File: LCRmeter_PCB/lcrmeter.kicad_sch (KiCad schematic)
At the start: 60 parts, among them J1 LCR_input, J2 LCR_input, J3 Prog_interface, J4 USB_B_Micro, J5 OSCILLOSCOPE, J6 misc, J7 misc, SW1 power, SW2 +, SW3 -, SW4 ok, SW5 back, U3 OLED, U4 74HC14, U5 MCP6001-OT, U6 STM32G473C_B-C-E_Tx, Y1 8Mhz

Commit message: some random schematic update
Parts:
- removed D1: 2V, Diode_SMD:D_MiniMELF, symbol Device:D_Zener
- removed J5: OSCILLOSCOPE, footprints:BNC TE CONNECTIVITY 5-1634503, symbol Connector:Conn_Coaxial
- removed R3: 10k, Resistor_SMD:R_0603_1608Metric_Pad1.05x0.95mm_HandSolder, symbol Device:R_Small
- removed R7: R, symbol Device:R
- added C16: 10u, Capacitor_SMD:C_0603_1608Metric_Pad1.05x0.95mm_HandSolder, symbol Device:C
- added C17: C_Polarized_Small, symbol Device:C_Polarized_Small
- added Q1: NX7002BKR, Package_TO_SOT_SMD:SOT-23, symbol Transistor_FET:2N7002
- added R20, R21, R8: 0, symbol Device:R
- added TP1, TP2, TP3: TestPoint, symbol Connector:TestPoint
- added U1, U2, U7: 74LVC1G66, symbol 74xGxx:74LVC1G66
- added U8: MCP6001-OT, Package_TO_SOT_SMD:SOT-23-5, symbol Amplifier_Operational:MCP6001-OT
- R17: value 10k -> 0; footprint Resistor_SMD:R_0603_1608Metric_Pad1.05x0.95mm_HandSolder -> (none)
- R18: value 10k -> 2k; footprint Resistor_SMD:R_0603_1608Metric_Pad1.05x0.95mm_HandSolder -> (none)
- R19: value 20k -> 500; footprint Resistor_SMD:R_0805_2012Metric_Pad1.15x1.40mm_HandSolder -> (none)
- R22, R23: footprint Resistor_SMD:R_0603_1608Metric_Pad1.05x0.95mm_HandSolder -> (none)
- SW2: value + -> up
- SW3: value - -> down
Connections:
- net +1V5: now also R21.2, R8.2, U8.1, U8.4 (-); no longer J1.3 (Pin_3), J1.4 (Pin_4), J2.3 (Pin_3), J2.4 (Pin_4), J6.4 (Pin_4), J7.4 (Pin_4), U5.1, U5.4 (-)
- net ADC_1: now also R18.1, R19.1, U5.1, U5.4 (-), R20.2, TP1.1, U7.1
- net ADC_2: now also Q1.3 (D), TP2.1, U1.2, U2.2, U7.2
- net GND: now also R17.2, R23.1, U6.19 (VSSA), U6.23 (VSS), U6.35 (VSS), U6.47 (VSS), Q1.2 (S), U1.3 (GND), U2.3 (GND), U8.2 (V-); no longer R18.2, R2.1, R23.2
- net OSCILLOSCOPE: no longer R17.2, R18.1
- net OSCILLOSCOPE_IN: now also J6.5 (Pin_5), J7.5 (Pin_5); no longer J6.3 (Pin_3), J7.3 (Pin_3), R17.1
- net PWM_OUT: now also J6.3 (Pin_3), J7.3 (Pin_3); no longer J6.1 (Pin_1), J7.1 (Pin_1)
- net RST: now also U6.7 (PG10)
- net USB_+: now also U6.34 (PA12)
- net USB_-: now also U6.33 (PA11)
- net VCC: now also J6.1 (Pin_1), J7.1 (Pin_1), R22.2, U6.1 (VBAT), U6.24 (VDD), U6.36 (VDD), U6.48 (VDD), U1.5 (VCC), U2.5 (VCC), U8.5 (V+); no longer J6.5 (Pin_5), J7.5 (Pin_5), R19.1, R22.1
- net VDDA: now also U6.21 (VDDA)
- net at C2.1, Y1.1: now also U6.5 (PF0)
- net at C1.1, Y1.2: now also U6.6 (PF1)
- net at R19.2: now also U1.1
- net at R2.2: now also U6.45 (PB8)
- net DAC_UNBUFFERED: now reaches U6.12 (PA4)
- net DAC_UNBUFFERED: now also U5.3 (+), R20.1
- net WAVE_OUT: now reaches U6.14 (PA6)
- net WAVE_OUT: now also J6.4 (Pin_4), J7.4 (Pin_4)
- net EVENTOUT: now reaches U6.2 (PC13)
- net EVENTOUT: now also TP3.1
- new net: J1.3 (Pin_3), J1.4 (Pin_4), J2.3 (Pin_3), J2.4 (Pin_4), R17.1, R8.1
- new net: R21.1, R22.1, R23.2, U8.3 (+)
- new net: R18.2, U2.1
- new net EN_PATH_1: U1.4
- new net EN_PATH_2: U2.4, U7.4
- new net RES_CALIBRATION: Q1.1 (G)
- no-connect marks 13 -> 12
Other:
- note added: "Use dac buffered, if uc's internal is not enough Use other paths for measurments if needed use Vdd/2 voltage reference if needed?"
- note removed: "Optional"
- moved on the sheet: C1, C10, C12, C13, C14, C15, C2, J1, J2, J7, R1, R10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

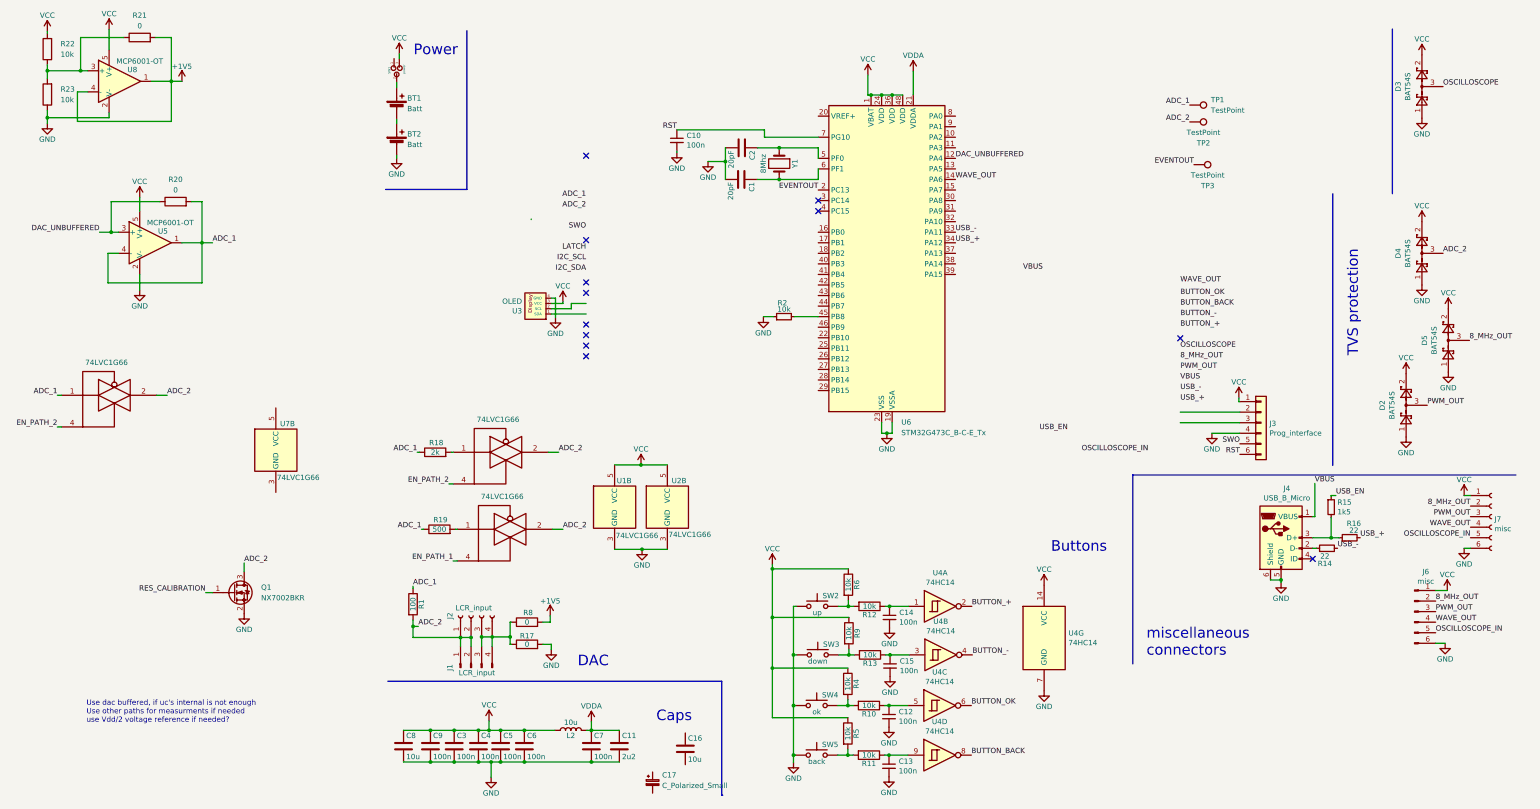
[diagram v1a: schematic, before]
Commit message: schematic done added generator for g4
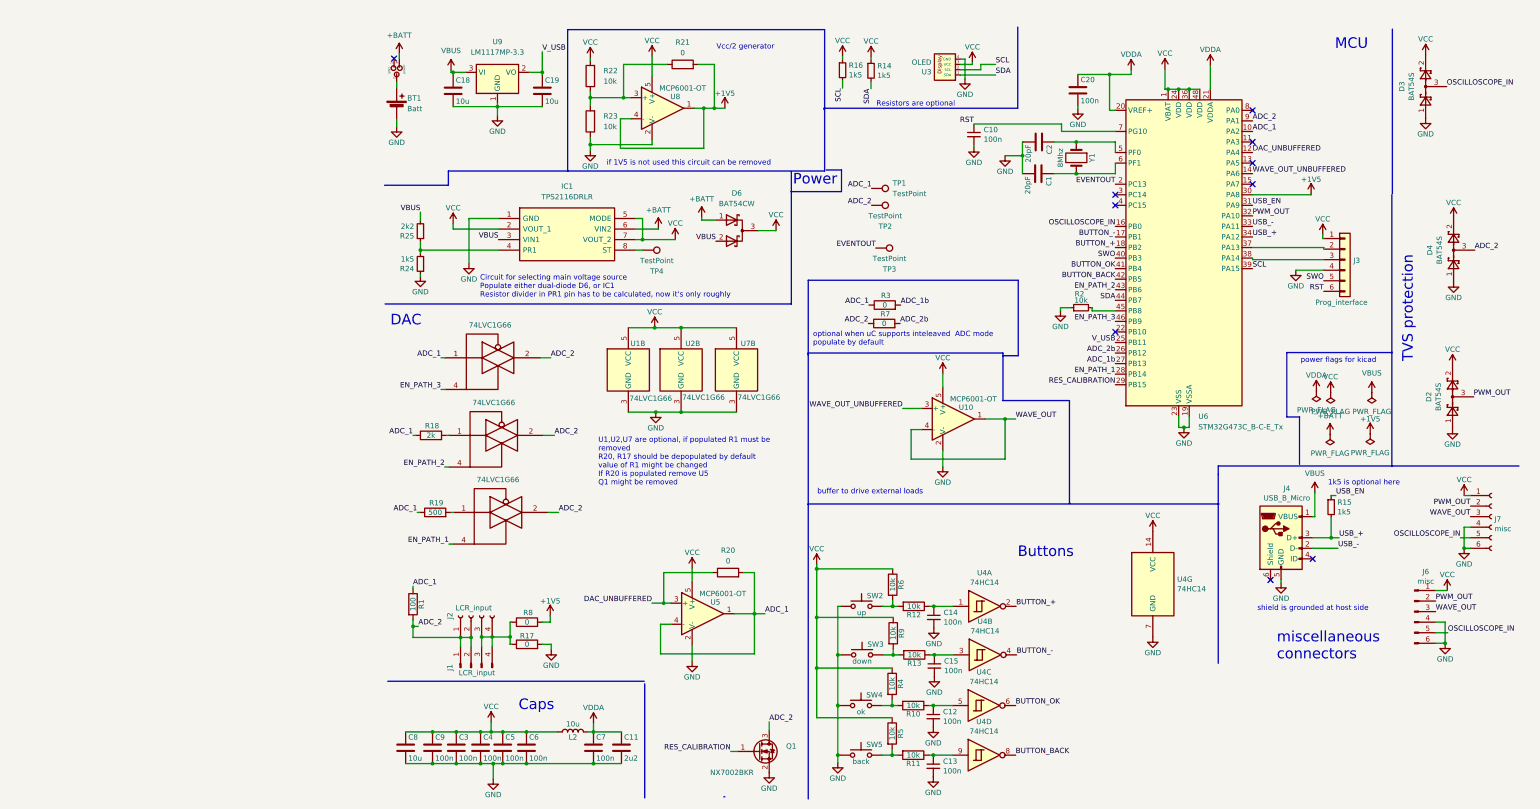
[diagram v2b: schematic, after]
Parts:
- removed BT2: Batt, Battery:BatteryHolder_Keystone_2466_1xAAA, symbol Device:Battery_Cell
- removed C16: 10u, Capacitor_SMD:C_0603_1608Metric_Pad1.05x0.95mm_HandSolder, symbol Device:C
- removed C17: C_Polarized_Small, symbol Device:C_Polarized_Small
- removed D5: BAT54S, Package_TO_SOT_SMD:SOT-23, symbol lcrmeter-rescue:BAT54S-Diode
- added C18, C19: 10u, Capacitor_SMD:C_0603_1608Metric_Pad1.05x0.95mm_HandSolder, symbol Device:C
- added C20: 100n, Capacitor_SMD:C_0603_1608Metric_Pad1.05x0.95mm_HandSolder, symbol Device:C
- added D6: BAT54CW, symbol Device:D_Schottky_Dual_CommonCathode_AAK_Parallel
- added IC1: TPS2116DRLR, SOTFL50P160X60-8N, symbol library_loader:TPS2116DRLR
- added R24: 1k5, Resistor_SMD:R_0805_2012Metric_Pad1.15x1.40mm_HandSolder, symbol Device:R_Small
- added R25: 2k2, Resistor_SMD:R_0805_2012Metric_Pad1.15x1.40mm_HandSolder, symbol Device:R_Small
- added R3, R7: 0, symbol Device:R
- added TP4: TestPoint, symbol Connector:TestPoint
- added U10: MCP6001-OT, Package_TO_SOT_SMD:SOT-23-5, symbol Amplifier_Operational:MCP6001-OT
- added U9: LM1117MP-3.3, Package_TO_SOT_SMD:SOT-223-3_TabPin2, symbol Regulator_Linear:LM1117MP-3.3
- R14, R16: value 22 -> 1k5
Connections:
- net 8_MHz_OUT is gone; now on net PWM_OUT: J6.2 (Pin_2), J7.2 (Pin_2)
- net OSCILLOSCOPE is gone; now on net OSCILLOSCOPE_IN: D3.3
- net +1V5: now also U6.30 (PA8)
- net ADC_1: now also U6.10 (PA2), R3.1
- net ADC_2: now also U6.9 (PA1), R7.1
- net BUTTON_+: now also U6.18 (PB2)
- net BUTTON_-: now also U6.17 (PB1)
- net BUTTON_BACK: now also U6.42 (PB5)
- net BUTTON_OK: now also U6.41 (PB4)
- net EN_PATH_1: now also U6.28 (PB14)
- net EN_PATH_2: now also U6.43 (PB6); no longer U7.4
- net GND: now also BT1.2 (-), J6.4 (Pin_4), J7.4 (Pin_4), R2.1, U7.3 (GND), C18.2, C19.2, C20.2, IC1.1 (GND), R24.1, U10.2 (V-), U9.1 (GND); no longer J4.6 (Shield)
- net OSCILLOSCOPE_IN: now also U6.16 (PB0)
- net PWM_OUT: now also U6.32 (PA10); no longer J6.3 (Pin_3), J7.3 (Pin_3)
- net RES_CALIBRATION: now also U6.29 (PB15)
- net SWO: now also U6.40 (PB3)
- net USB_+: now also J4.3 (D+), R15.2; no longer R16.2
- net USB_-: now also J4.2 (D-); no longer R14.2
- net USB_EN: now also U6.31 (PA9)
- net VBUS: now also C18.1, D6.2 (K), IC1.3 (VIN1), R25.2, U9.3 (VI)
- net VCC: now also R14.1, R16.1, U7.5 (VCC), D6.3 (A), IC1.2 (VOUT_1), IC1.5 (MODE), IC1.7 (VOUT_2), U10.5 (V+); no longer SW1.3
- net VDDA: now also U6.20 (VREF+), C20.1
- net WAVE_OUT: now also J6.3 (Pin_3), J7.3 (Pin_3), U10.1, U10.4 (-); no longer J6.4 (Pin_4), J7.4 (Pin_4), U6.14 (PA6)
- net at J3.2 (Pin_2): now also U6.37 (PA13)
- net at J3.3 (Pin_3): now also U6.38 (PA14)
- net SDA: now reaches U3.1 (SDA)
- net SDA: now also R14.2, U6.44 (PB7)
- net SCL: now reaches U3.2 (SCL)
- net SCL: now also R16.2, U6.39 (PA15)
- net V_USB: now reaches U6.25 (PB11)
- net V_USB: now also C19.1, U9.2 (VO)
- net ADC_2b: now reaches U6.26 (PB12)
- net ADC_2b: now also R7.2
- net ADC_1b: now reaches U6.27 (PB13)
- net ADC_1b: now also R3.2
- net EN_PATH_3: now reaches U6.46 (PB9)
- net EN_PATH_3: now also U7.4
- new net: IC1.4 (PR1), R24.2, R25.1
- new net: IC1.8 (ST), TP4.1
- new net +BATT: D6.1 (K), IC1.6 (VIN2), SW1.3
- new net WAVE_OUT_UNBUFFERED: U10.3 (+), U6.14 (PA6)
- no-connect marks 12 -> 10
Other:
- note added: "1k5 is optional here"
- note added: "Circuit for selecting main voltage source Populate either dual-diode D6, or IC1 Resistor divider in PR1 pin has to be calculated, now it's only roughly"
- note added: "MCU"
- note added: "Resistors are optional"
- note added: "U1,U2,U7 are optional, if populated R1 must be removed R20, R17 should be depopulated by default value of R1 might be changed If R20 is populated remove U5 Q1 might be removed"
- note added: "Vcc/2 generator"
- note added: "buffer to drive external loads"
- note added: "if 1V5 is not used this circuit can be removed"
- note added: "optional when uC supports inteleaved ADC mode populate by default"
- note added: "power flags for kicad"
- note added: "shield is grounded at host side"
- note removed: "Use dac buffered, if uc's internal is not enough Use other paths for measurments if needed use Vdd/2 voltage reference if needed?"
- moved on the sheet: C1, C10, C11, C12, C13, C14, C15, C2, C3, C4, C5, C6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

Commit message: placed components on PCB
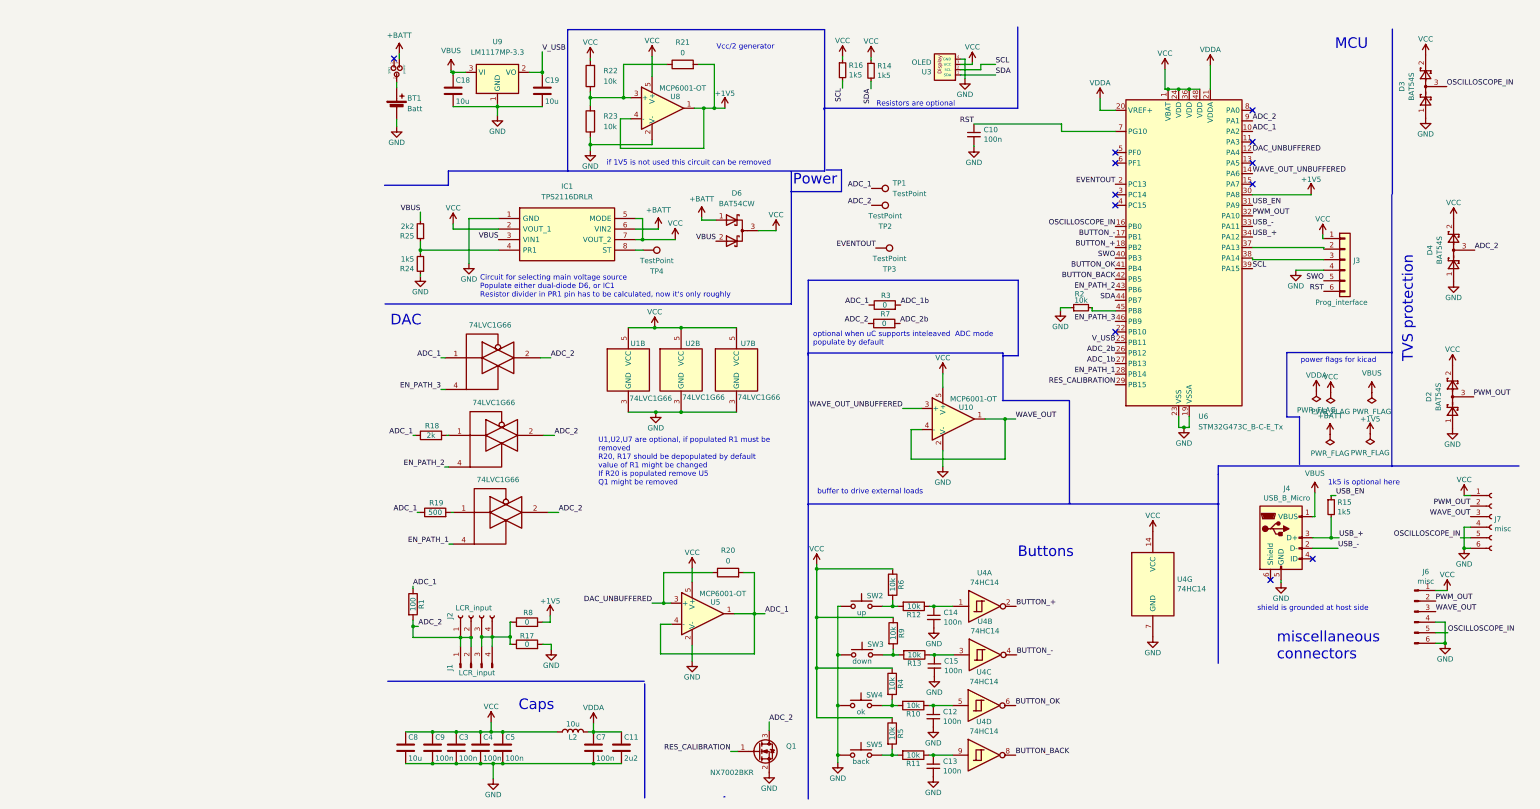
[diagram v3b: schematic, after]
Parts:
- removed C1, C2: 20pF, Capacitor_SMD:C_0805_2012Metric_Pad1.15x1.40mm_HandSolder, symbol Device:C
- removed C20, C6: 100n, Capacitor_SMD:C_0603_1608Metric_Pad1.05x0.95mm_HandSolder, symbol Device:C
- removed Y1: 8Mhz, Crystal:Crystal_HC49-U_Vertical, symbol Device:Crystal
- BT1: footprint Battery:BatteryHolder_Keystone_2466_1xAAA -> Battery:BatteryHolder_Keystone_2468_2xAAA
- C10, C12, C13, C14, C15, C3, C4, C5, C7, C9: footprint Capacitor_SMD:C_0603_1608Metric_Pad1.05x0.95mm_HandSolder -> Capacitor_SMD:C_0603_1608Metric_Pad1.08x0.95mm_HandSolder
- C11: footprint Capacitor_SMD:C_0805_2012Metric_Pad1.15x1.40mm_HandSolder -> Capacitor_SMD:C_0603_1608Metric_Pad1.08x0.95mm_HandSolder
- C18, C19, C8: footprint Capacitor_SMD:C_0603_1608Metric_Pad1.05x0.95mm_HandSolder -> Capacitor_SMD:C_0805_2012Metric_Pad1.18x1.45mm_HandSolder
- D6: footprint (none) -> Package_TO_SOT_SMD:SOT-23
- IC1: footprint SOTFL50P160X60-8N -> Library_Loader:SOTFL50P160X60-8N
- R1, R14, R15, R16, R24, R25: footprint Resistor_SMD:R_0805_2012Metric_Pad1.15x1.40mm_HandSolder -> Resistor_SMD:R_0805_2012Metric_Pad1.20x1.40mm_HandSolder
- R10, R11, R12, R13, R2, R4, R5, R6, R9: footprint Resistor_SMD:R_0603_1608Metric_Pad1.05x0.95mm_HandSolder -> Resistor_SMD:R_0603_1608Metric_Pad0.98x0.95mm_HandSolder
- R17, R18, R19, R20, R21, R22, R23, R3, R7, R8: footprint (none) -> Resistor_SMD:R_0805_2012Metric_Pad1.20x1.40mm_HandSolder
- TP1, TP2, TP3, TP4: footprint (none) -> TestPoint:TestPoint_Pad_1.0x1.0mm
- U1, U2, U7: footprint (none) -> Package_TO_SOT_SMD:SOT-23-5
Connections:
- no-connect marks 10 -> 12
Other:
- company: (none) -> Rafał Mazurkiewicz

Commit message: routing mostly done
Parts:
- removed TP1, TP2: TestPoint, TestPoint:TestPoint_Pad_1.0x1.0mm, symbol Connector:TestPoint
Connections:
- net VBUS: no longer D6.2 (K), IC1.3 (VIN1), R25.2
- net V_USB: now also D6.2 (K), IC1.3 (VIN1), R25.2
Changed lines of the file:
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@@
     (effects (font (size 1.27 1.27)) (justify left bottom))
   )
-  (label "ADC_2" (at 129.159 54.864 180) (fields_autoplaced)
-    (effects (font (size 1.27 1.27)) (justify right bottom))
-  )
   (label "WAVE_OUT" (at 273.304 129.794 180) (fields_autoplaced)
     (effects (font (size 1.27 1.27)) (justify right bottom))
@@
     (effects (font (size 1.27 1.27)) (justify left bottom))
   )
-  (label "ADC_1" (at 129.159 50.8 180) (fields_autoplaced)
-    (effects (font (size 1.27 1.27)) (justify right bottom))
-  )
   (label "SDA" (at 159.004 23.495 0) (fields_autoplaced)
     (effects (font (size 1.27 1.27)) (justify left bottom))
@@
     (effects (font (size 1.27 1.27)) (justify left bottom))
   )
-  (label "VBUS" (at 39.37 63.119 180) (fields_autoplaced)
+  (label "V_USB" (at 39.37 63.119 180) (fields_autoplaced)
     (effects (font (size 1.27 1.27)) (justify right bottom))
   )
@@
     (effects (font (size 1.27 1.27)) (justify right bottom))
   )
-  (label "VBUS" (at 91.694 63.5 180) (fields_autoplaced)
+  (label "V_USB" (at 91.694 63.5 180) (fields_autoplaced)
     (effects (font (size 1.27 1.27)) (justify right bottom))
   )
@@
     (effects (font (size 1.27 1.27)) (justify left bottom))
   )
-  (label "VBUS" (at 20.574 56.515 180) (fields_autoplaced)
+  (label "V_USB" (at 20.574 56.515 180) (fields_autoplaced)
     (effects (font (size 1.27 1.27)) (justify right bottom))
   )
@@
     )
   )
-  (symbol (lib_id "Connector:TestPoint") (at 129.159 50.8 270) (unit 1)
-    (in_bom yes) (on_board yes) (dnp no)
-    (property "Reference" "TP1" (at 134.239 49.53 90)
-      (effects (font (size 1.27 1.27)) (justify left))
-    )
-    (property "Value" "TestPoint" (at 134.239 52.07 90)
-      (effects (font (size 1.27 1.27)) (justify left))
-    )
-    (property "Footprint" "TestPoint:TestPoint_Pad_1.0x1.0mm" (at 129.159 55.88 0)
-      (effects (font (size 1.27 1.27)) hide)
-    )
-    (property "Datasheet" "~" (at 129.159 55.88 0)
-      (effects (font (size 1.27 1.27)) hide)
-    )
-    (pin "1")
-    (instances
-      (project "lcrmeter"
-        (path "/cf9a12ad-2fa3-4d0e-8bc4-f65b698e427e"
-          (reference "TP1") (unit 1)
-        )
-      )
-    )
-  )
   (symbol (lib_id "74xGxx:74LVC1G66") (at 41.148 128.778 0) (unit 1)
     (in_bom yes) (on_board yes) (dnp no) (fields_autoplaced)
@@
         )
       )
-    )
-  )
-  (symbol (lib_id "Connector:TestPoint") (at 129.159 54.864 270) (unit 1)
-    (in_bom yes) (on_board yes) (dnp no)
-    (property "Reference" "TP2" (at 132.461 59.944 90)
-      (effects (font (size 1.27 1.27)))
-    )
-    (property "Value" "TestPoint" (at 132.461 57.404 90)
-      (effects (font (size 1.27 1.27)))
-    )
-    (property "Footprint" "TestPoint:TestPoint_Pad_1.0x1.0mm" (at 129.159 59.944 0)
-      (effects (font (size 1.27 1.27)) hide)
-    )
-    (property "Datasheet" "~" (at 129.159 59.944 0)
-      (effects (font (size 1.27 1.27)) hide)
-    )
-    (pin "1")
-    (instances
-      (project "lcrmeter"
-        (path "/cf9a12ad-2fa3-4d0e-8bc4-f65b698e427e"
-          (reference "TP2") (unit 1)
-        )
-      )

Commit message: added some notes on PCB
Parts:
- U5, U8: value MCP6001-OT -> LMH6645
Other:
- note added: "TODO in next version Needs to add 100nF cap for every op amp, and IC R20 is not needed. Add testpoint on DAC_UNBUFFERED net due to series resistance on op amps output, it might not work 1v5"
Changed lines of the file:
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@@
     (effects (font (size 1.27 1.27)) (justify left bottom))
   )
+  (text "TODO in next version\nNeeds to add 100nF cap for every op amp, and IC\nR20 is not needed.\nAdd testpoint on DAC_UNBUFFERED net\ndue to series resistance on op amps output, it might not work 1v5\n\n"
+    (at 111.125 62.611 0)
+    (effects (font (size 1.27 1.27) (color 255 0 63 1)) (justify left bottom))
+  )
   (text "optional when uC supports inteleaved  ADC mode\npopulate by default"
     (at 115.062 88.773 0)
@@
       (effects (font (size 1.27 1.27)))
     )
-    (property "Value" "MCP6001-OT" (at 83.693 26.67 0)
+    (property "Value" " LMH6645" (at 83.693 26.67 0)
       (effects (font (size 1.27 1.27)))
     )
@@
       (effects (font (size 1.27 1.27)))
     )
-    (property "Value" "MCP6001-OT" (at 93.345 148.336 0)
+    (property "Value" " LMH6645" (at 93.345 148.336 0)
       (effects (font (size 1.27 1.27)))
     )
